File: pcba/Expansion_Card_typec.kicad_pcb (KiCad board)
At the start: 2 copper layers, 26 x 30 mm, 7 parts, among them P1 USB_C_Plug_USB2.0, U1 AP2112K-3.3

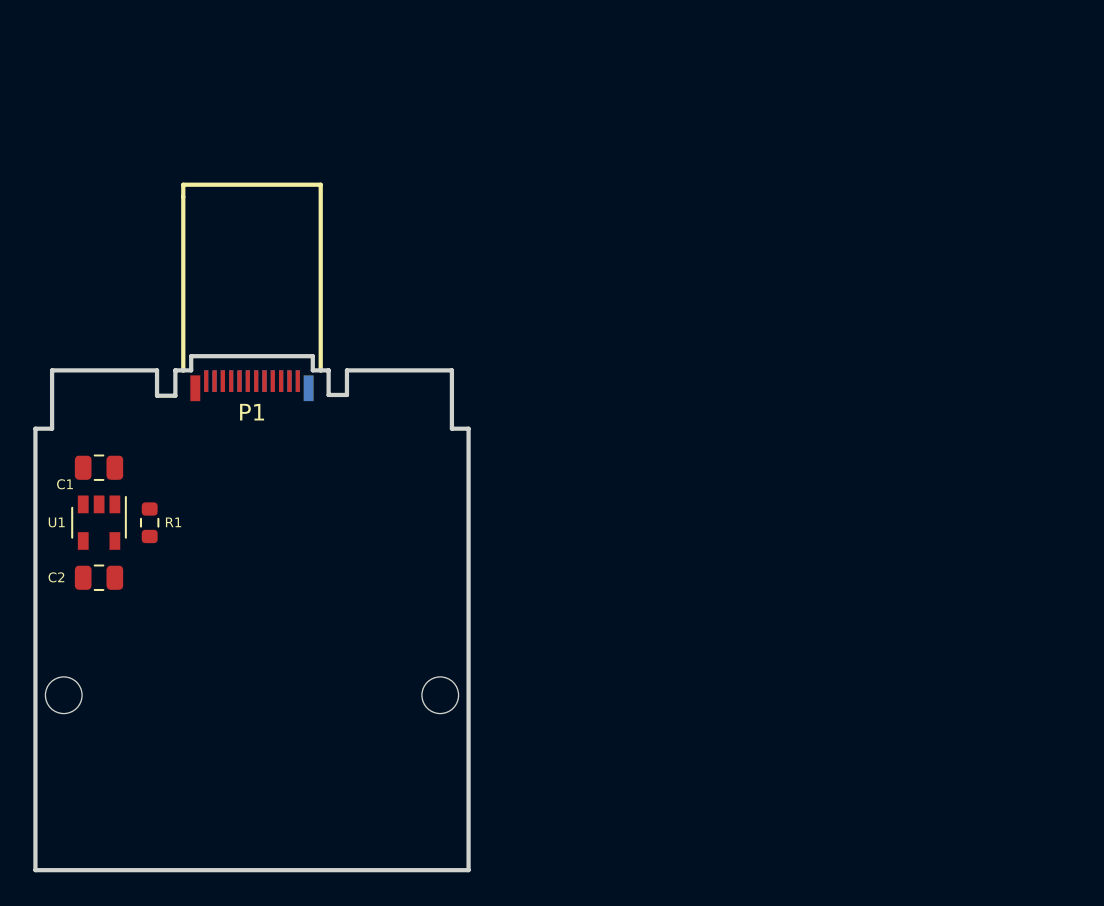
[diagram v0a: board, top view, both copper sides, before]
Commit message: revise edge cuts
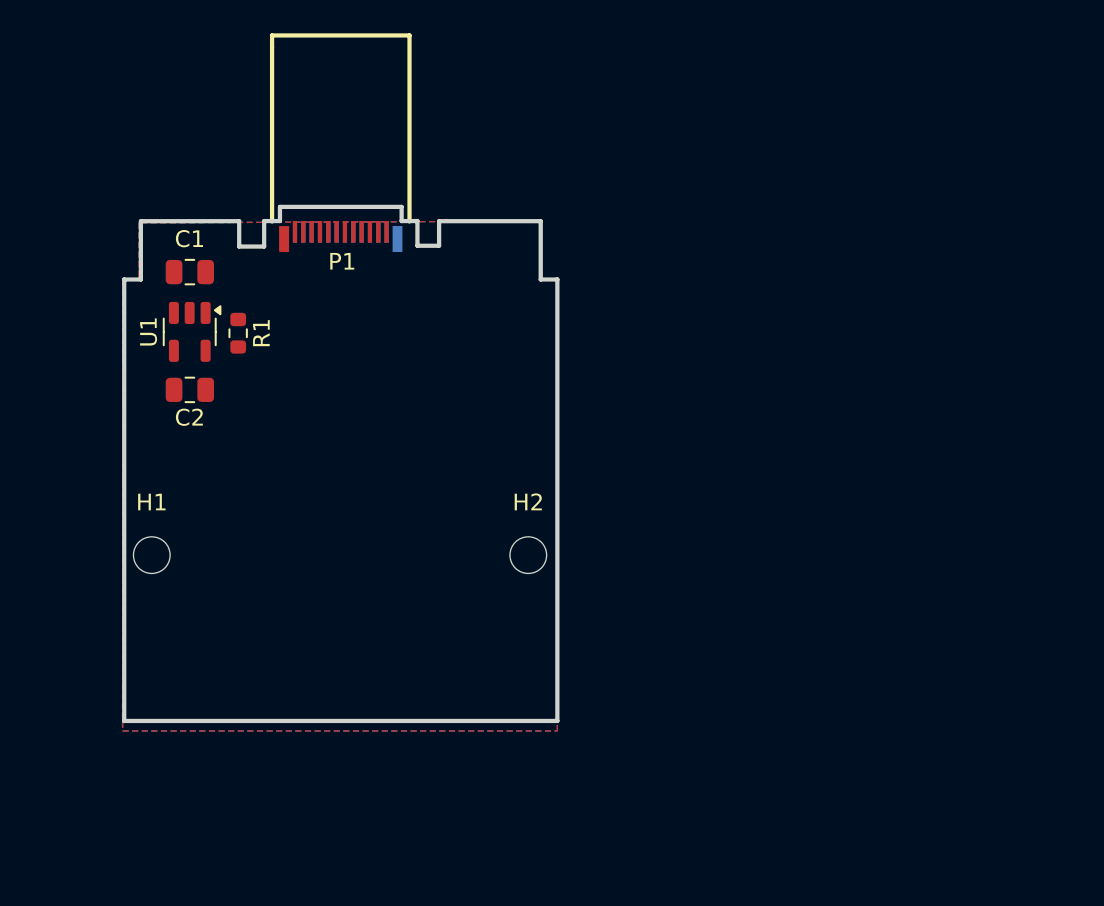
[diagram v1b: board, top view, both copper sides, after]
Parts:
- P1: footprint Expansion_Card:TYPEC-SMD_TYPEC-950-ARP24 -> easytypec:TYPEC-SMD_TYPEC-950-ARP24
- moved C1 12.9 mm to (136.3, 121.1)
- moved U1 12.7 mm to (136.3, 124.7)
- moved R1 12.6 mm to (139.2, 124.8)
- moved C2 12.5 mm to (136.3, 128.2)
- moved P1 10.4 mm to (145.3, 118.9)
- moved H1 9.93 mm to (134.0, 138.1)
- moved H2 9.93 mm to (156.6, 138.1)
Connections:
- net /USB_DN renamed /USB_D-
- net /USB_DP renamed /USB_D+
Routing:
- added copper zone on B.Cu, net +3.3V
- added copper zone on F.Cu, net +3.3V
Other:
- outline, holes or cut-outs redrawn

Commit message: revise edge cuts more
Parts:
- moved P1 0.82 mm to (145.2, 119.7)
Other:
- outline, holes or cut-outs redrawn
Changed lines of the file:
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@@
 	(footprint "easytypec:TYPEC-SMD_TYPEC-950-ARP24"
 		(layer "F.Cu")
-		(at 145.33 118.898566 180)
+		(at 145.23 119.7125 180)
 		(property "Reference" "P1"
 			(at -0.084817 -1.5875 0)
@@
 			)
 			(layer "F.SilkS")
-			(net 1)
 		)
 		(fp_line
@@
 			)
 			(layer "F.SilkS")
-			(net 1)
 		)
 		(fp_line
@@
 			)
 			(layer "F.SilkS")
-			(net 1)
 		)
 		(fp_line
@@
 			)
 			(layer "F.SilkS")
-			(net 1)
 		)
 		(fp_poly
@@
 			(fill yes)
 			(layer "Dwgs.User")
-			(net 1)
 		)
 		(fp_line
@@
 			)
 			(layer "Edge.Cuts")
-			(net 1)
 		)
 		(fp_line
@@
 			)
 			(layer "Edge.Cuts")
-			(net 1)
 		)
 		(fp_line
@@
 			)
 			(layer "Edge.Cuts")
-			(net 1)
 		)
 		(fp_line
@@
 			)
 			(layer "Edge.Cuts")
-			(net 1)
 		)
 		(fp_line
@@
 			)
 			(layer "Edge.Cuts")
-			(net 1)
 		)
 		(fp_line
@@
 			)
 			(layer "Edge.Cuts")
-			(net 1)
 		)
 		(fp_line
@@
 			)
 			(layer "Edge.Cuts")
-			(net 1)
 		)
 		(fp_poly
@@
 			(fill yes)
 			(layer "User.1")
-			(net 1)
 		)
 		(fp_poly
@@
 			(fill yes)
 			(layer "User.1")
-			(net 1)
 		)
 		(fp_poly
@@
 			(fill yes)
 			(layer "User.1")
-			(net 1)
 		)
 		(fp_poly
@@
 			(fill yes)
 			(layer "User.1")
-			(net 1)
 		)
 		(fp_poly
@@
 			(fill yes)
 			(layer "User.1")
-			(net 1)
 		)
 		(fp_poly
@@
 			(fill yes)
 			(layer "User.1")
-			(net 1)
 		)
 		(fp_poly
@@
 			(fill yes)
 			(layer "User.1")
-			(net 1)
 		)
 		(fp_poly
@@
 			(fill yes)
 			(layer "User.1")
-			(net 1)
 		)
 		(fp_poly
@@
 			(fill yes)
 			(layer "User.1")
-			(net 1)
 		)
 		(fp_poly
@@
 			(fill yes)
 			(layer "User.1")
-			(net 1)
 		)
 		(fp_poly
@@
 			(fill yes)
 			(layer "User.1")
-			(net 1)
 		)
 		(fp_poly
@@
 			(fill yes)
 			(layer "User.1")
-			(net 1)
 		)
 		(fp_poly
@@
 			(fill yes)
 			(layer "User.1")
-			(net 1)
 		)
 		(fp_poly
@@
 			(fill yes)
 			(layer "User.1")
-			(net 1)
 		)
 		(fp_poly
@@
 			(fill yes)
 			(layer "User.1")
-			(net 1)
 		)
 		(fp_poly
@@
 			(fill yes)
 			(layer "User.1")
-			(net 1)
 		)
 		(fp_poly
@@
 			(fill yes)
 			(layer "User.1")
-			(net 1)
 		)
 		(fp_poly
@@
 			(fill yes)
 			(layer "User.1")
-			(net 1)
 		)
 		(fp_poly
@@
 			(fill yes)
 			(layer "User.1")
-			(net 1)
 		)
 		(fp_poly
@@
 			(fill yes)
 			(layer "User.1")
-			(net 1)
 		)
 		(fp_poly
@@
 			(fill yes)
 			(layer "User.1")
-			(net 1)
 		)
 		(fp_poly
@@
 			(fill yes)
 			(layer "User.1")
-			(net 1)
 		)
 		(fp_poly
@@
 			(fill yes)
 			(layer "User.1")
-			(net 1)
 		)
 		(fp_poly
@@
 			(fill yes)
 			(layer "User.1")
-			(net 1)
 		)
 		(fp_poly
@@
 			(fill yes)
 			(layer "User.1")
-			(net 1)
 		)
 		(fp_poly
@@
 			(fill yes)
 			(layer "User.1")
-			(net 1)
 		)
 		(fp_line
@@
 			)
 			(layer "User.2")
-			(net 1)
 		)
 		(fp_line
@@
 			)
 			(layer "User.2")
-			(net 1)
 		)
 		(fp_line
@@
 			)
 			(layer "User.2")
-			(net 1)
 		)
 		(fp_line
@@
 			)
 			(layer "User.2")
-			(net 1)
 		)
 		(fp_poly
@@
 			(fill yes)
 			(layer "User.3")
-			(net 1)
 		)
 		(pad "25" smd rect
@@
 	)
 	(gr_line
+		(start 151.23 120.3745)
+		(end 149.83 120.3745)
+		(stroke
+			(width 0.254)
+			(type solid)
+		)
+		(layer "Edge.Cuts")
+	)
+	(gr_line
 		(start 139.23 118.043566)
 		(end 133.33 118.043566)
+		(stroke
+			(width 0.254)
+			(type solid)
+		)
+		(layer "Edge.Cuts")
+	)
+	(gr_line
+		(start 140.63 120.3745)
+		(end 139.23 120.3745)
 		(stroke
 			(width 0.254)
@@
 	)
 	(gr_line
-		(start 139.23 119.565566)
-		(end 139.23 118.043566)
+		(start 132.33 148.043566)
+		(end 158.33 148.043566)
 		(stroke
 			(width 0.254)
@@
 	)
 	(gr_line
-		(start 132.33 148.043566)
-		(end 158.33 148.043566)
+		(start 139.23 118.043566)
+		(end 139.23 120.3745)
+		(stroke
+			(width 0.254)
+			(type solid)
+		)
+		(layer "Edge.Cuts")
+	)
+	(gr_line
+		(start 151.23 118.043566)
+		(end 151.23 120.3745)
 		(stroke
 			(width 0.254)
@@
 	)
 	(gr_line
-		(start 149.93 119.519566)
-		(end 151.23 119.519566)
-		(stroke
-			(width 0.254)
-			(type solid)
-		)
-		(layer "Edge.Cuts")
-	)
-	(gr_line
-		(start 151.23 119.519566)
-		(end 151.23 118.043566)
-		(stroke
-			(width 0.254)
-			(type solid)
-		)
-		(layer "Edge.Cuts")
-	)
-	(gr_line
 		(start 132.33 121.543566)
 		(end 132.33 148.043566)
@@
 		(start 158.33 121.543566)
 		(end 158.33 148.043566)
-		(stroke
-			(width 0.254)
-			(type solid)
-		)
-		(layer "Edge.Cuts")
-	)
-	(gr_line
-		(start 140.73 119.565566)
-		(end 139.23 119.565566)
 		(stroke
 			(width 0.254)
@@
 		(polygon
 			(pts
-				(xy 149.84 120.22) (xy 140.84 120.22) (xy 140.830296 118.073566) (xy 149.830296 118.073566)
-			)
-		)
+				(xy 149.70913 120.9) (xy 140.70913 120.9) (xy 140.696578 118.123566) (xy 149.696578 118.123566)
+			)
+		)

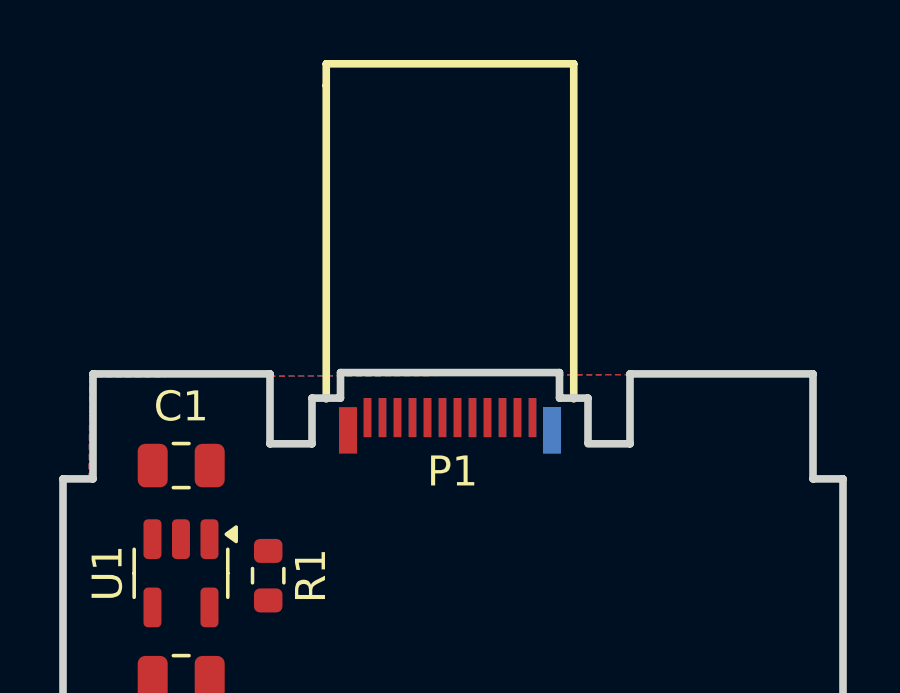
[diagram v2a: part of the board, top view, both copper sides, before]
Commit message: put usb more below
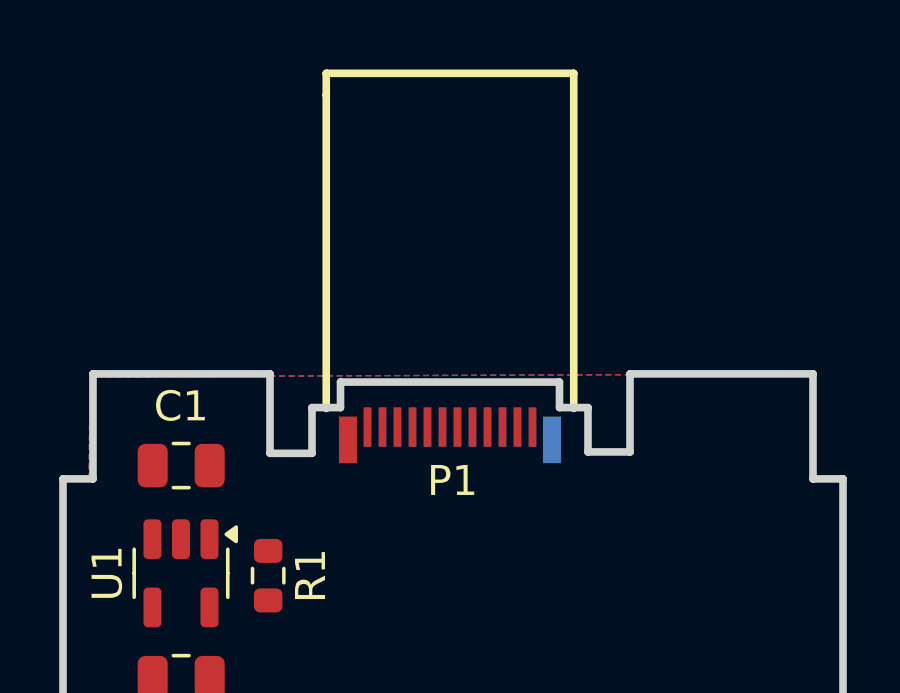
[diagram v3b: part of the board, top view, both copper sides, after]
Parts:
- moved P1 0.32 mm to (145.2, 120.0)
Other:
- outline, holes or cut-outs redrawn

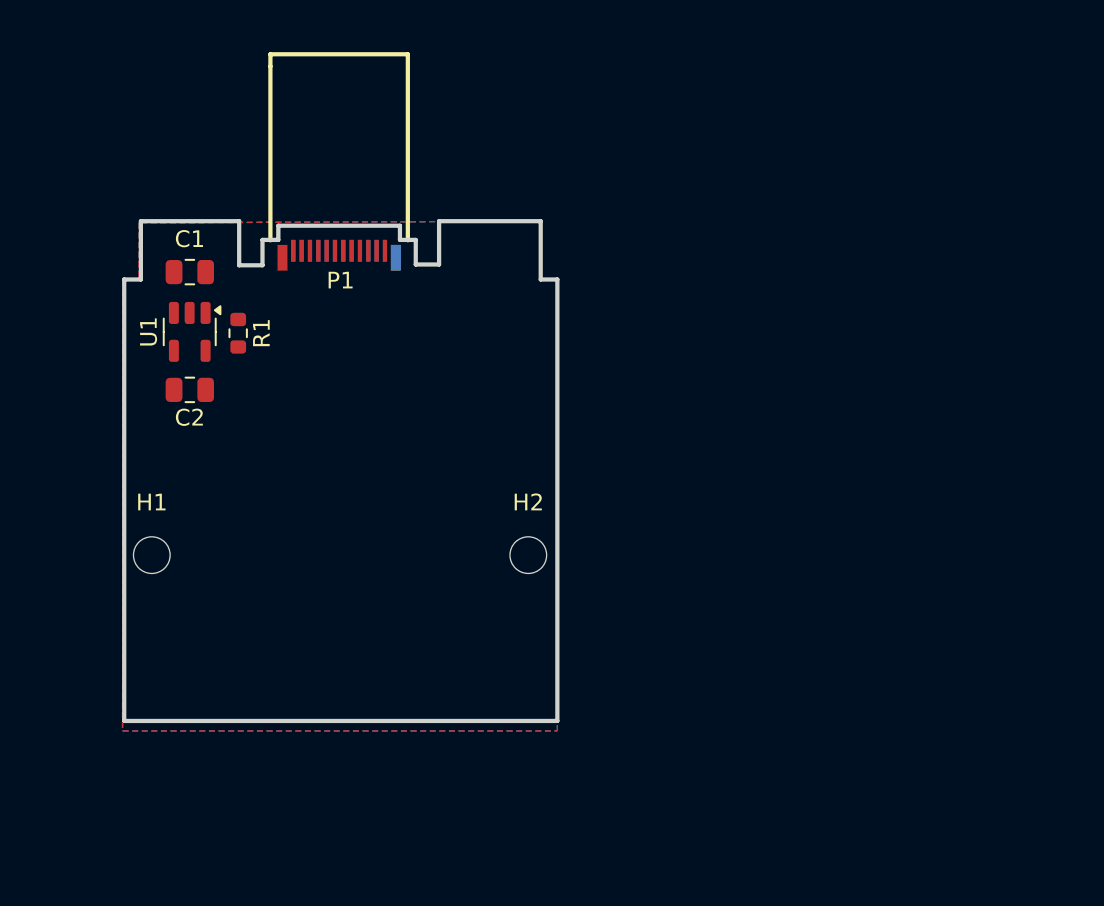
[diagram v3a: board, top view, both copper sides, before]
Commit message: lower type-c
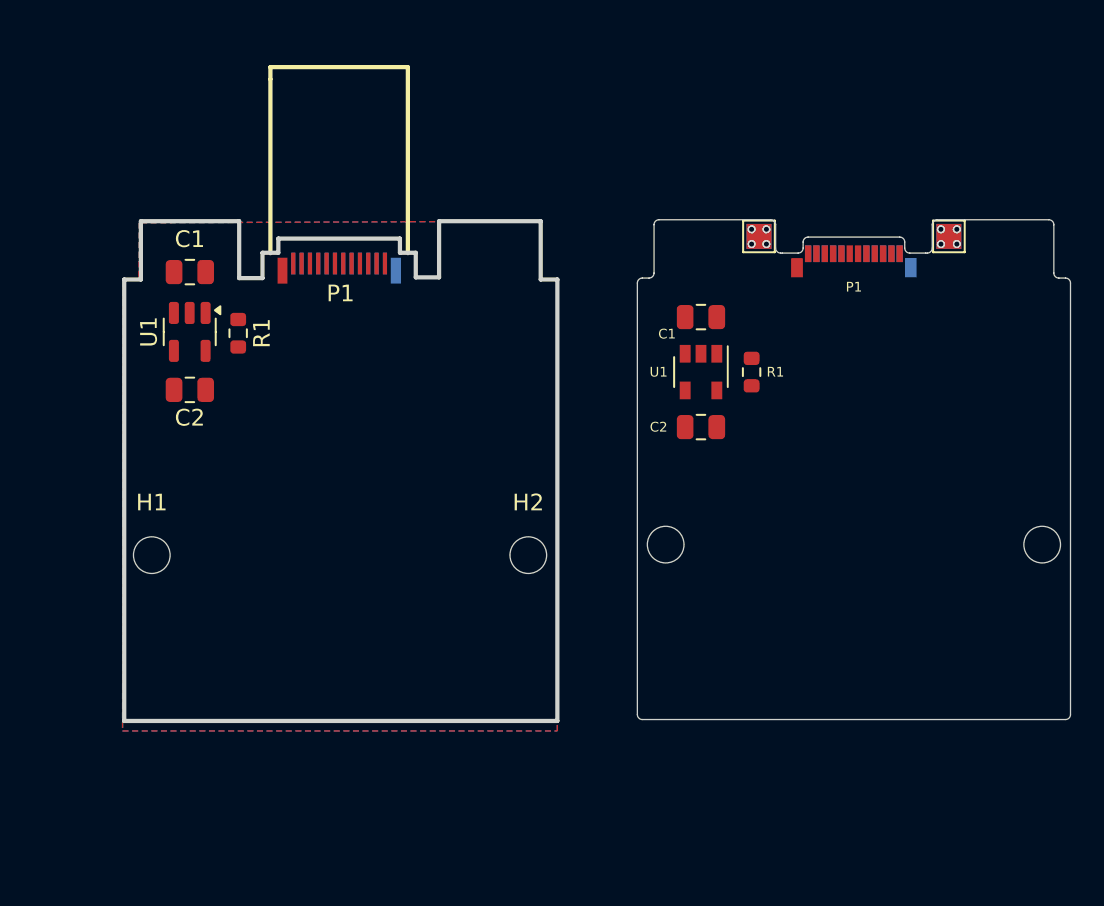
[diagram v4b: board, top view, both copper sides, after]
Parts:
- added C1: 10uF, Capacitor_SMD:C_0805_2012Metric, F.Cu at (166.9, 123.8)
- added C2: 10uF, Capacitor_SMD:C_0805_2012Metric, F.Cu at (166.9, 130.4)
- added H1: MountingHole, MountingHole:MountingHole_2.2mm_M2, F.Cu at (164.8, 137.5)
- added H2: MountingHole, MountingHole:MountingHole_2.2mm_M2, F.Cu at (187.4, 137.5)
- added P1: USB_C_Plug_USB2.0, Expansion_Card:USB_C_Plug_Molex_105444, F.Cu at (176.1, 120.0)
- added R1: 5.1k, Resistor_SMD:R_0603_1608Metric, F.Cu at (170.0, 127.1)
- added TP1: TestPoint, TestPoint:TestPoint_Pad_1.5x1.5mm, F.Cu at (170.4, 119.0)
- added TP2: TestPoint, TestPoint:TestPoint_Pad_1.5x1.5mm, B.Cu at (170.4, 119.0)
- added TP3: TestPoint, TestPoint:TestPoint_Pad_1.5x1.5mm, F.Cu at (181.8, 119.0)
- added TP4: TestPoint, TestPoint:TestPoint_Pad_1.5x1.5mm, B.Cu at (181.8, 119.0)
- added U1: AP2112K-3.3, Package_TO_SOT_SMD:SOT-23-5, F.Cu at (166.9, 127.1)
- moved P1 0.77 mm to (145.2, 120.8)
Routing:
- net GND: vias 0 -> 8
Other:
- board size 26 x 30 mm -> 56.8 x 30.1 mm

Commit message: minor fix
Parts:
- removed the C1 at (166.9, 123.8)
- removed the C2 at (166.9, 130.4)
- removed the H1 at (164.8, 137.5)
- removed the H2 at (187.4, 137.5)
- removed the P1 at (176.1, 120.0)
- removed the R1 at (170.0, 127.1)
- removed TP1, TP2, TP3, TP4: TestPoint, TestPoint:TestPoint_Pad_1.5x1.5mm
- removed the U1 at (166.9, 127.1)
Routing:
- net GND: vias 8 -> 0
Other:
- board size 56.8 x 30.1 mm -> 26 x 30 mm

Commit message: fix size
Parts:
- moved P1 1.13 mm to (145.2, 121.9)
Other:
- outline, holes or cut-outs redrawn
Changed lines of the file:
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@@
 	(footprint "easytypec:TYPEC-SMD_TYPEC-950-ARP24"
 		(layer "F.Cu")
-		(at 145.23 120.8 180)
+		(at 145.23 121.93 180)
 		(property "Reference" "P1"
 			(at -0.084817 -1.5875 0)
@@
 	)
 	(gr_line
-		(start 140.63 121.462)
-		(end 139.23 121.462)
+		(start 140.63 122.592)
+		(end 139.23 122.592)
 		(stroke
 			(width 0.254)
@@
 	(gr_line
 		(start 151.23 118.043566)
-		(end 151.23 121.416)
+		(end 151.23 122.546)
 		(stroke
 			(width 0.254)
@@
 	)
 	(gr_line
-		(start 149.83 121.416)
-		(end 151.23 121.416)
+		(start 149.83 122.546)
+		(end 151.23 122.546)
 		(stroke
 			(width 0.254)
@@
 	(gr_line
 		(start 139.23 118.043566)
-		(end 139.23 121.462)
-		(stroke
-			(width 0.254)
+		(end 139.23 122.592)
+		(stroke
+			(width 0.254)
